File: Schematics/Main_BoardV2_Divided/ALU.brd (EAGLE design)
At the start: 146 x 166 mm, 32 parts

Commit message: Routd and Cams Created
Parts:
- moved ALU1:IC4 2.84 mm to (88.9, 95.2)
- moved ALU1:IC7 2.84 mm to (43.2, 44.5)
- moved B_REGISTER1:IC3 2.84 mm to (43.2, 95.2)
- moved B_REGISTER1:IC8 2.84 mm to (43.2, 128.3)
- moved ALU1:IC8 2.84 mm to (22.9, 44.5)
- moved B_REGISTER1:IC2 2.84 mm to (22.9, 95.2)
- moved B_REGISTER1:IC7 2.84 mm to (22.9, 128.3)
- moved ALU1:V1 2.84 mm to (88.9, 43.2)
- moved A_REGISTER1:IC1 2.84 mm to (113.0, 125.7)
- moved A_REGISTER1:IC2 2.84 mm to (113.0, 95.2)
- moved A_REGISTER1:IC3 2.84 mm to (68.6, 95.2)
- moved A_REGISTER1:IC7 2.84 mm to (68.6, 128.3)
- moved A_REGISTER1:IC8 2.84 mm to (87.6, 128.3)
- moved ALU1:D1 2.84 mm to (43.2, 19.1)
- moved ALU1:D2 2.84 mm to (22.9, 19.1)
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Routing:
- net VCC: track 0.00 -> 361.4 mm, vias 0 -> 5
- net 8B_4: track 0.00 -> 225.3 mm
- net SUB: track 0.00 -> 213.8 mm
- net 8B_2: track 0.00 -> 193.4 mm, vias 0 -> 2
- net ALU1:A_10: track 0.00 -> 189.7 mm, vias 0 -> 4
- net N$20: track 0.00 -> 187.9 mm
- net CLK: track 0.00 -> 183.7 mm, vias 0 -> 4
- net 8B_1: track 0.00 -> 182.1 mm, vias 0 -> 3
- net 8B_3: track 0.00 -> 180.6 mm, vias 0 -> 5
- net ALU1:A_11: track 0.00 -> 179.7 mm, vias 0 -> 1
- net ALU1:A_9: track 0.00 -> 174.6 mm, vias 0 -> 3
- net N$21: track 0.00 -> 162.6 mm, vias 0 -> 4
- net ALU1:A_12: track 0.00 -> 160.1 mm, vias 0 -> 3
- net N$19: track 0.00 -> 157.4 mm, vias 0 -> 4
- net CLR: track 0.00 -> 152.4 mm, vias 0 -> 6
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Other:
- board size 146 x 166 mm -> 135.9 x 166 mm
- board text added: "8Bit Bus"
- board text added: "Control Signals"
- board text added: "Flags"

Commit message: Visual Improvments
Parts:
- SV18: device con-lstb:MA08-1 -> pinhead:1X08
- SV24: device con-lstb:MA03-1 -> pinhead:1X03
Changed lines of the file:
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@@
 </layers>
 <board>
-<fusionsync huburn="a.cGVyc29uYWw6dWUyYzAxZDJj" projecturn="a.cGVyc29uYWw6dWUyYzAxZDJjIzIwMTkwNTA1MTkyMDg5NTI2" f3durn="urn:adsk.wipprod:dm.lineage:mhiw1OJTQqKmMQQ8zRvthA" pcbguid="d4c267fc-dfac-4531-b3ec-d435942649d2" lastpulledtime="" lastsyncedchangeguid="f80efb56-7c03-6c29-5f04-4ecde63bf9ba"/>
+<fusionsync huburn="a.cGVyc29uYWw6dWUyYzAxZDJj" projecturn="a.cGVyc29uYWw6dWUyYzAxZDJjIzIwMTkwNTA1MTkyMDg5NTI2" f3durn="urn:adsk.wipprod:dm.lineage:mhiw1OJTQqKmMQQ8zRvthA" pcbguid="d4c267fc-dfac-4531-b3ec-d435942649d2" lastpulledtime="" lastsyncedchangeguid="31de29da-6829-9adc-e3e0-53290fd6633f"/>
 <plain>
 <wire x1="2.54" y1="2.54" x2="138.41" y2="2.54" width="0" layer="20"/>
@@
 <attribute name="VALUE" x="43.18" y="128.27" size="1.27" layer="27" ratio="10" rot="R270"/>
 </element>
-<element name="SV18" library="con-lstb" library_urn="urn:adsk.eagle:library:162" package="MA08-1" package3d_urn="urn:adsk.eagle:package:8343/1" value="" x="129.54" y="123.19" smashed="yes" rot="R90">
+<element name="SV18" library="pinhead" library_urn="urn:adsk.eagle:library:325" package="1X08" package3d_urn="urn:adsk.eagle:package:22409/2" value="" x="129.54" y="123.19" smashed="yes" rot="R90">
 <attribute name="MF" value="" x="129.54" y="123.19" size="1.778" layer="27" rot="R90" display="off"/>
 <attribute name="MPN" value="" x="129.54" y="123.19" size="1.778" layer="27" rot="R90" display="off"/>
@@
 <attribute name="VALUE" x="129.54" y="123.19" size="1.27" layer="27" ratio="10" rot="R90"/>
 </element>
-<element name="SV24" library="con-lstb" library_urn="urn:adsk.eagle:library:162" package="MA03-1" package3d_urn="urn:adsk.eagle:package:8339/1" value="" x="129.54" y="50.8" smashed="yes" rot="R270">
+<element name="SV24" library="pinhead" library_urn="urn:adsk.eagle:library:325" package="1X03" package3d_urn="urn:adsk.eagle:package:22458/2" value="" x="129.54" y="50.8" smashed="yes" rot="R270">
 <attribute name="MF" value="" x="129.54" y="50.8" size="1.778" layer="27" rot="R270" display="off"/>
 <attribute name="MPN" value="" x="129.54" y="50.8" size="1.778" layer="27" rot="R270" display="off"/>

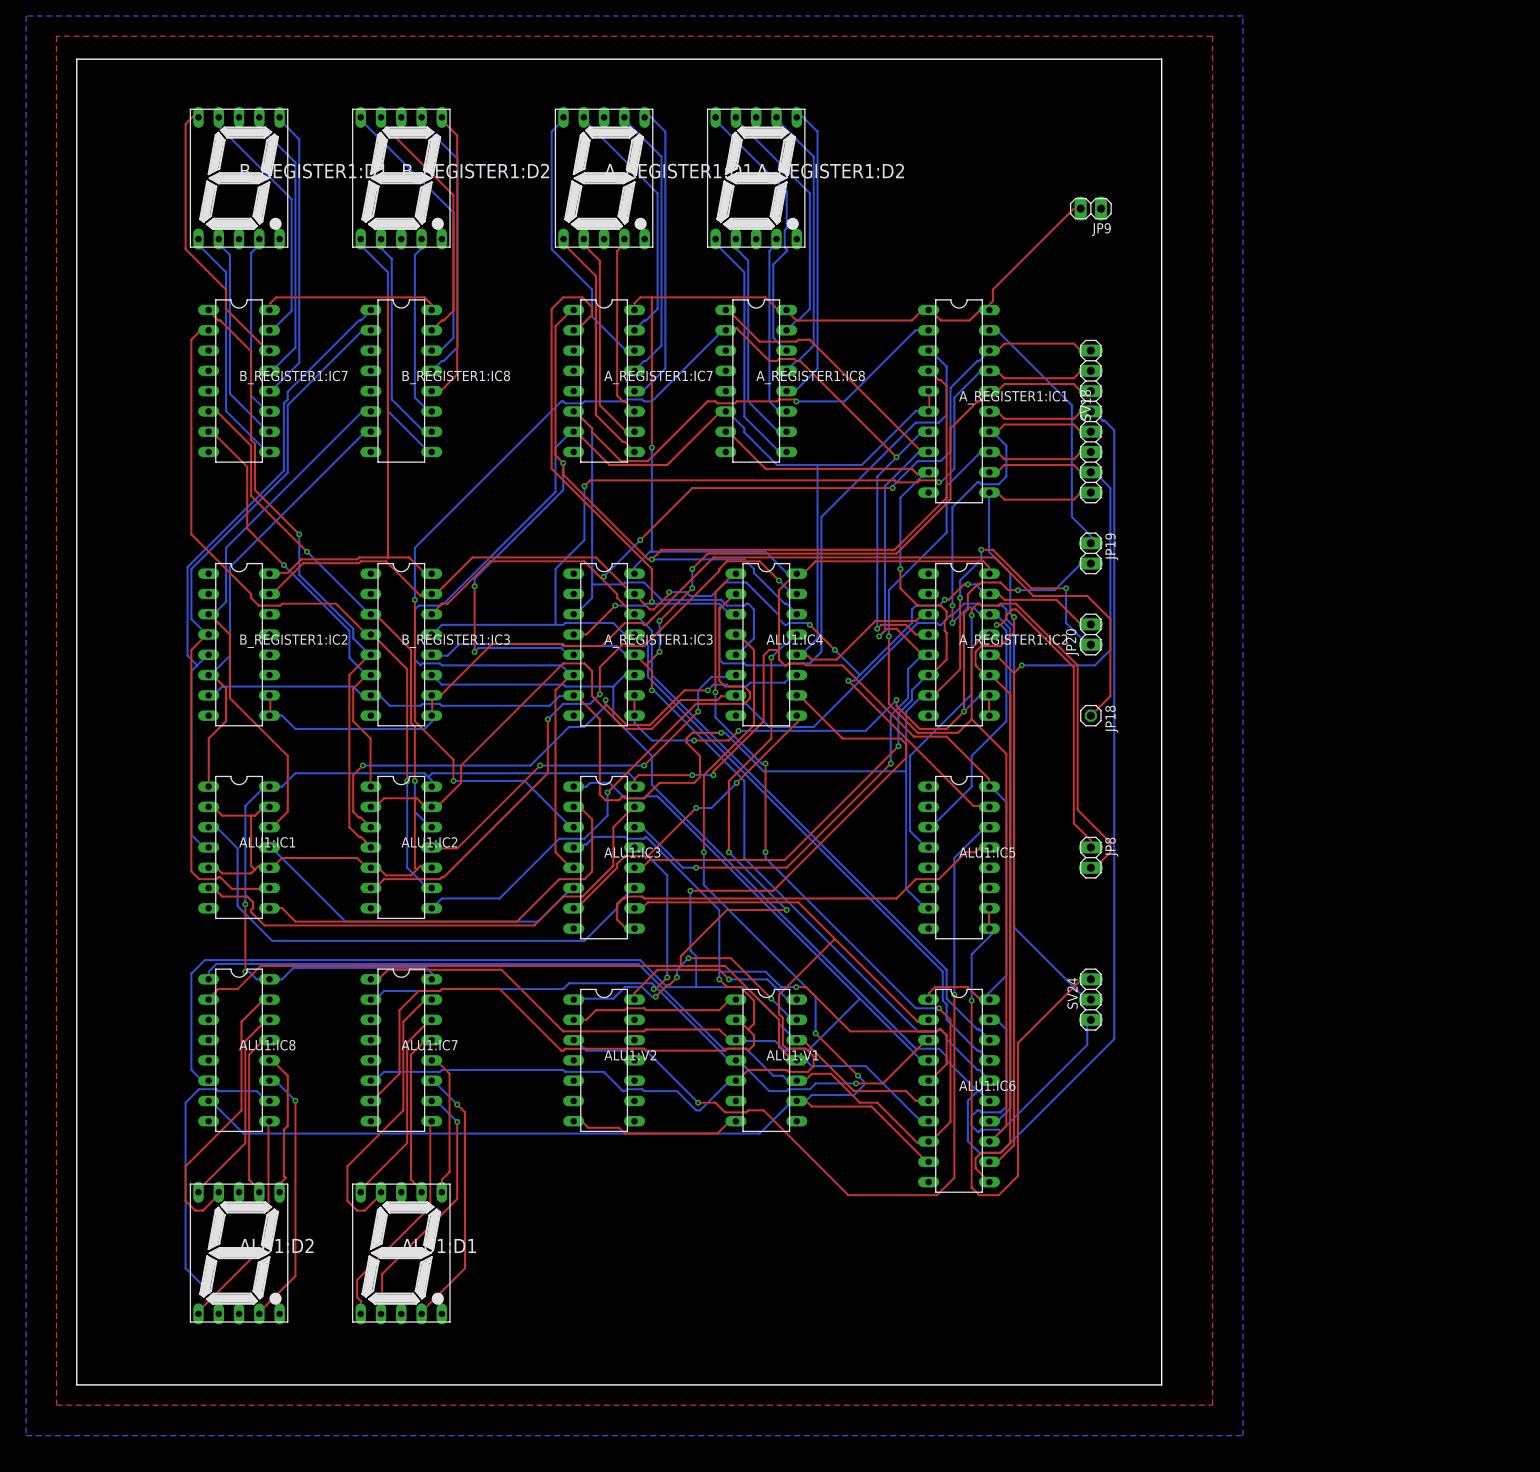
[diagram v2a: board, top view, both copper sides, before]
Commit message: Microcode Added and Ram Updated
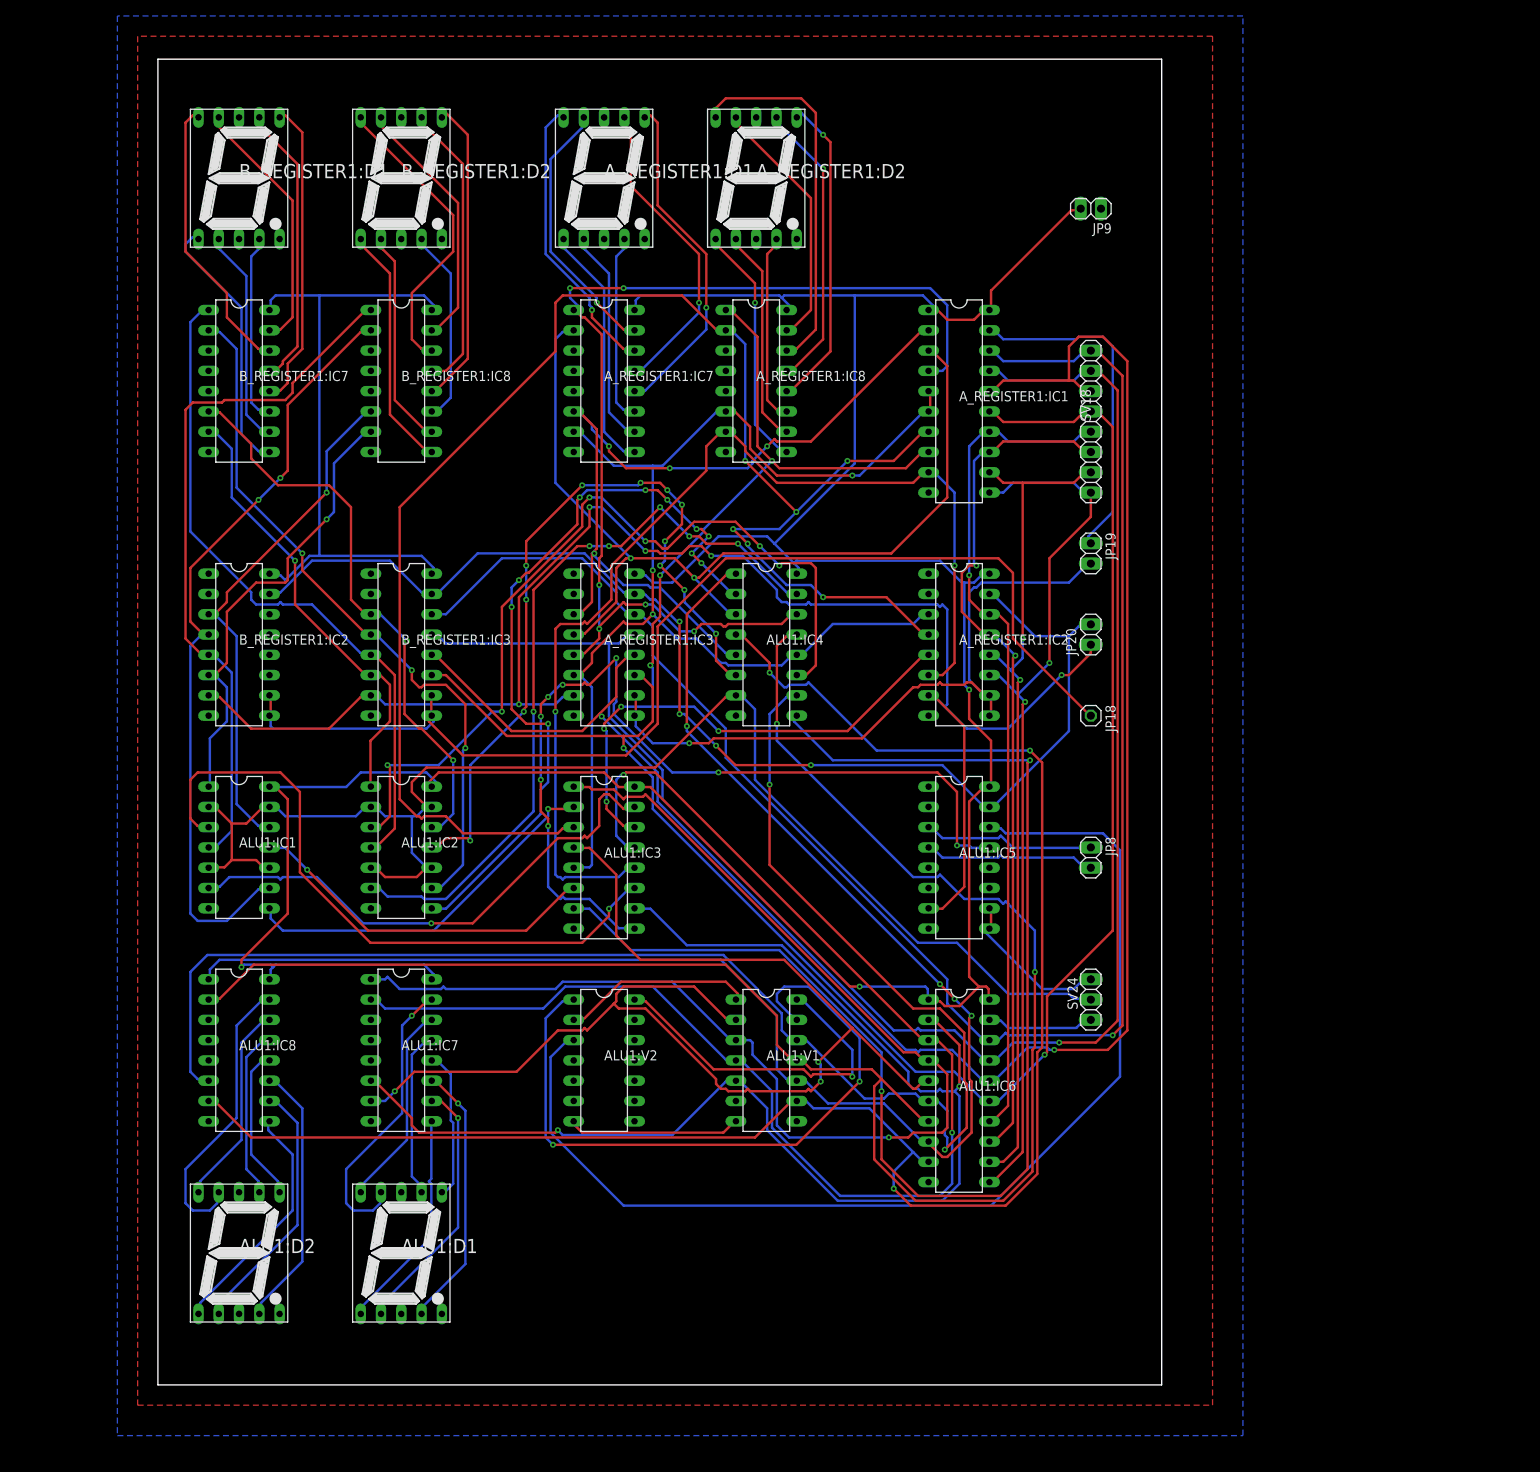
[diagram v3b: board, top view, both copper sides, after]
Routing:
- net ALU1:N$9: track 39.1 -> 164.8 mm
- net ALU1:A_15: track 100.0 -> 171.7 mm, vias 3 -> 2
- net ALU1:A_12: track 160.1 -> 224.2 mm, vias 3 -> 2
- net ALU1:N$25: track 54.4 -> 113.6 mm, vias 0 -> 8
- net CF: track 79.4 -> 21.6 mm, vias 1 -> 0
- net 8B_3: track 180.6 -> 236.9 mm, vias 5 -> 2
- net |FL: track 72.6 -> 20.2 mm, vias 1 -> 0
- net ALU1:N$19: track 34.8 -> 85.8 mm, vias 4 -> 2
- net ALU1:N$1: track 48.7 -> 96.3 mm, vias 3 -> 12
- net ALU1:A_9: track 174.6 -> 221.2 mm
- net ZF: track 67.6 -> 21.7 mm, vias 1 -> 0
- net N$21: track 162.6 -> 204.6 mm, vias 4 -> 6
- net 8B_1: track 182.1 -> 222.8 mm, vias 3 -> 1
- net ALU1:N$20: track 103.1 -> 140.9 mm, vias 2 -> 0
- net SUB: track 213.8 -> 176.5 mm
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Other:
- board size 135.9 x 166 mm -> 125.7 x 166 mm
